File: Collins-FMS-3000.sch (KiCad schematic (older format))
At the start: 25 parts, among them U2 MCP23017_SO, U3 MCP23017_SO, U4 IS31FL3733B

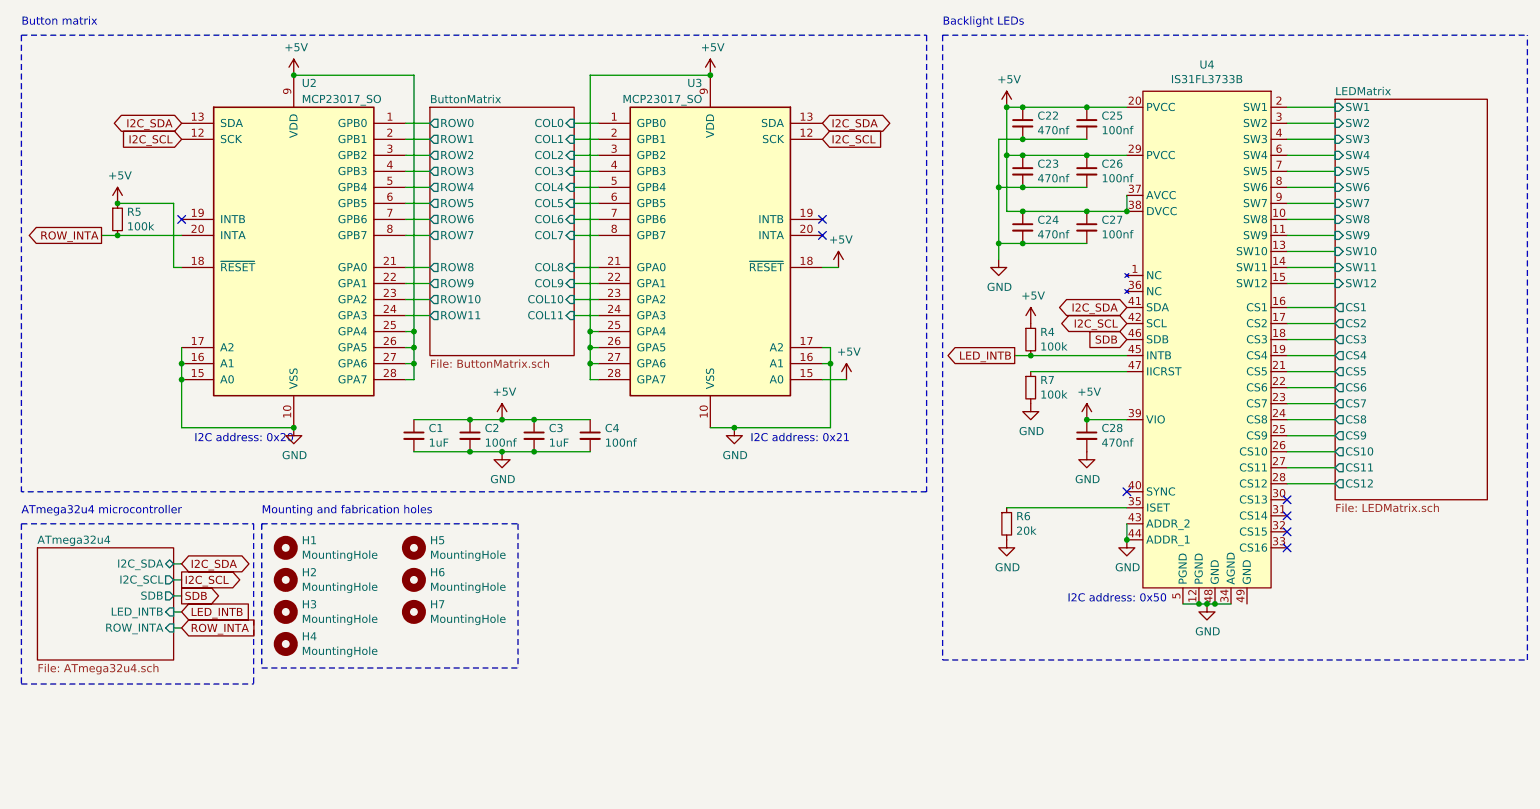
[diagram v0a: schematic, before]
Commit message: Get rid of interrupt pullups, add row pullups
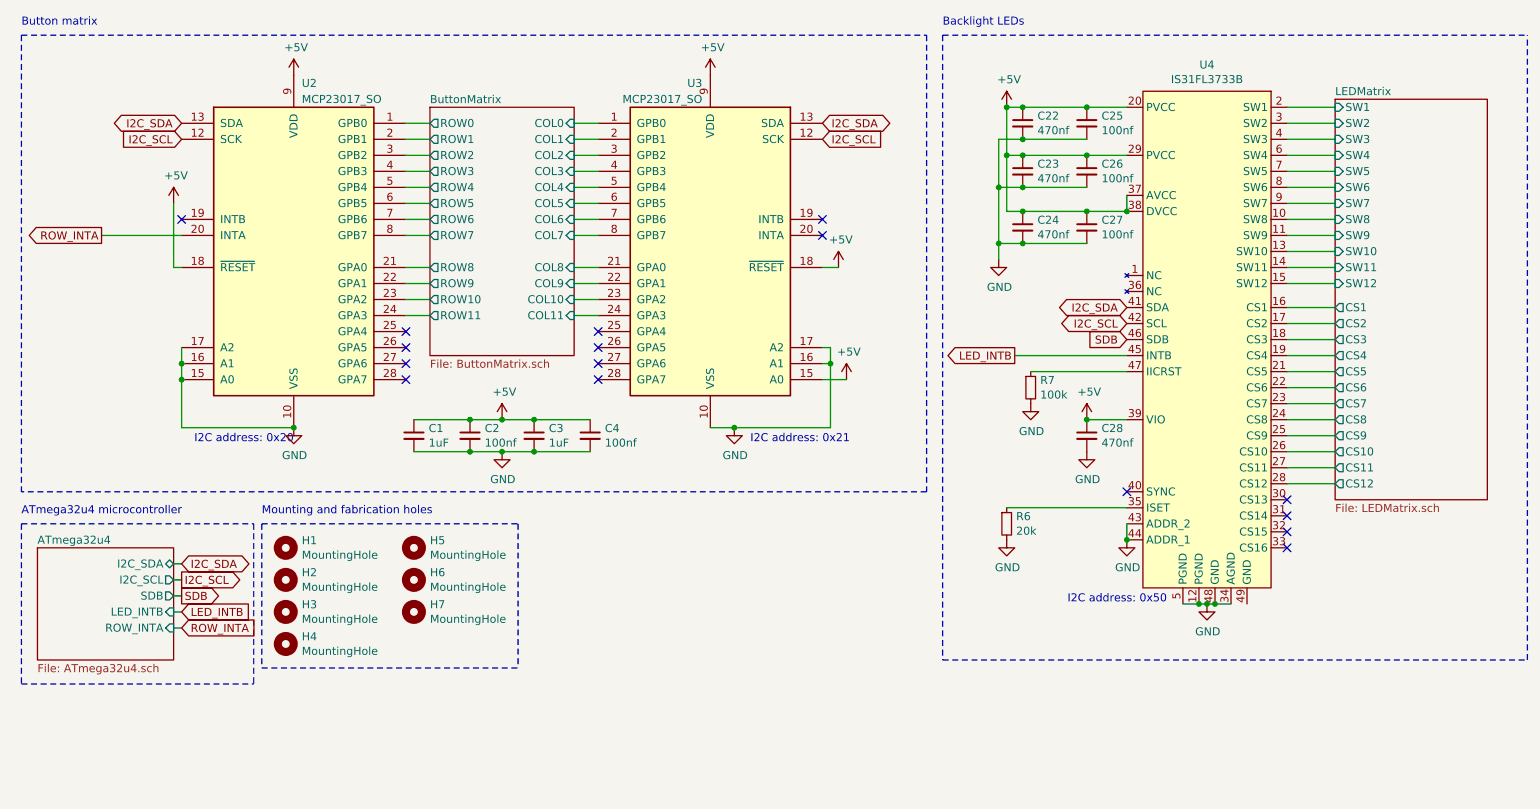
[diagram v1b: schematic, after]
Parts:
- removed R4, R5: 100k, Resistor_SMD:R_0402_1005Metric, symbol Device:R_Small
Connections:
- net +5V: no longer U2.25 (GPA4), U2.26 (GPA5), U2.27 (GPA6), U2.28 (GPA7), U3.25 (GPA4), U3.26 (GPA5), U3.27 (GPA6), U3.28 (GPA7)
- no-connect marks 8 -> 16
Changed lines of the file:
@@
 Text GLabel 6750 2650 0    50   Output ~ 0
 LED_INTB
-Wire Wire Line
-	7450 2650 6850 2650
-$Comp
-L Device:R_Small R4
-U 1 1 61926829
-P 6850 2550
-F 0 "R4" H 6909 2596 50  0000 L CNN
-F 1 "100k" H 6909 2505 50  0000 L CNN
-F 2 "Resistor_SMD:R_0402_1005Metric" H 6850 2550 50  0001 C CNN
-F 3 "~" H 6850 2550 50  0001 C CNN
-	1    6850 2550
-	1    0    0    -1
-$EndComp
-$Comp
-L power:+5V #PWR017
-U 1 1 61927283
-P 6850 2450
-F 0 "#PWR017" H 6850 2300 50  0001 C CNN
-F 1 "+5V" H 6865 2623 50  0000 C CNN
-F 2 "" H 6850 2450 50  0001 C CNN
-F 3 "" H 6850 2450 50  0001 C CNN
-	1    6850 2450
-	1    0    0    -1
-$EndComp
 Text GLabel 1550 4250 2    50   Input ~ 0
 LED_INTB
@@
 ROW_INTA
 $Comp
-L Device:R_Small R5
-U 1 1 619594D7
-P 1150 1800
-F 0 "R5" H 1209 1846 50  0000 L CNN
-F 1 "100k" H 1209 1755 50  0000 L CNN
-F 2 "Resistor_SMD:R_0402_1005Metric" H 1150 1800 50  0001 C CNN
-F 3 "~" H 1150 1800 50  0001 C CNN
-	1    1150 1800
-	1    0    0    -1
-$EndComp
-Wire Wire Line
-	6750 2650 6850 2650
-Connection ~ 6850 2650
-$Comp
 L power:+5V #PWR011
 U 1 1 619844EF
-P 1150 1700
-F 0 "#PWR011" H 1150 1550 50  0001 C CNN
-F 1 "+5V" H 1165 1873 50  0000 C CNN
-F 2 "" H 1150 1700 50  0001 C CNN
-F 3 "" H 1150 1700 50  0001 C CNN
-	1    1150 1700
+P 1500 1700
+F 0 "#PWR011" H 1500 1550 50  0001 C CNN
+F 1 "+5V" H 1515 1873 50  0000 C CNN
+F 2 "" H 1500 1700 50  0001 C CNN
+F 3 "" H 1500 1700 50  0001 C CNN
+	1    1500 1700
 	1    0    0    -1
 $EndComp
@@
 	1550 4350 1500 4350
 Wire Wire Line
-	1050 1900 1150 1900
-Connection ~ 1150 1700
-Connection ~ 1150 1900
-Wire Wire Line
-	1150 1900 1550 1900
-Wire Wire Line
 	1500 1700 1500 2100
 Wire Wire Line
 	1500 2100 1550 2100
-Wire Wire Line
-	1150 1700 1500 1700
-Wire Wire Line
-	2950 2800 3000 2800
-Wire Wire Line
-	3000 2800 3000 2700
-Wire Wire Line
-	3000 2500 2950 2500
-Wire Wire Line
-	2950 2600 3000 2600
-Connection ~ 3000 2600
-Wire Wire Line
-	3000 2600 3000 2500
-Wire Wire Line
-	2950 2700 3000 2700
-Connection ~ 3000 2700
-Wire Wire Line
-	3000 2700 3000 2600
-Wire Wire Line
-	3000 2500 3000 900
-Wire Wire Line
-	3000 900  2250 900
-Connection ~ 3000 2500
-Connection ~ 2250 900
-Wire Wire Line
-	4150 2800 4100 2800
-Wire Wire Line
-	4100 2800 4100 2700
-Wire Wire Line
-	4100 2500 4150 2500
-Wire Wire Line
-	4150 2600 4100 2600
-Connection ~ 4100 2600
-Wire Wire Line
-	4100 2600 4100 2500
-Wire Wire Line
-	4150 2700 4100 2700
-Connection ~ 4100 2700
-Wire Wire Line
-	4100 2700 4100 2600
-Wire Wire Line
-	4100 2500 4100 900
-Wire Wire Line
-	4100 900  4850 900
-Connection ~ 4100 2500
-Connection ~ 4850 900
 Wire Wire Line
 	2950 2400 3100 2400
@@
 Wire Wire Line
 	4000 2400 4150 2400
+NoConn ~ 2950 2500
+NoConn ~ 2950 2600
+NoConn ~ 2950 2700
+NoConn ~ 2950 2800
+NoConn ~ 4150 2500
+NoConn ~ 4150 2600
+NoConn ~ 4150 2700
+NoConn ~ 4150 2800
+Wire Wire Line
+	1050 1900 1550 1900
+Wire Wire Line
+	6750 2650 7450 2650
 $EndSCHEMATC

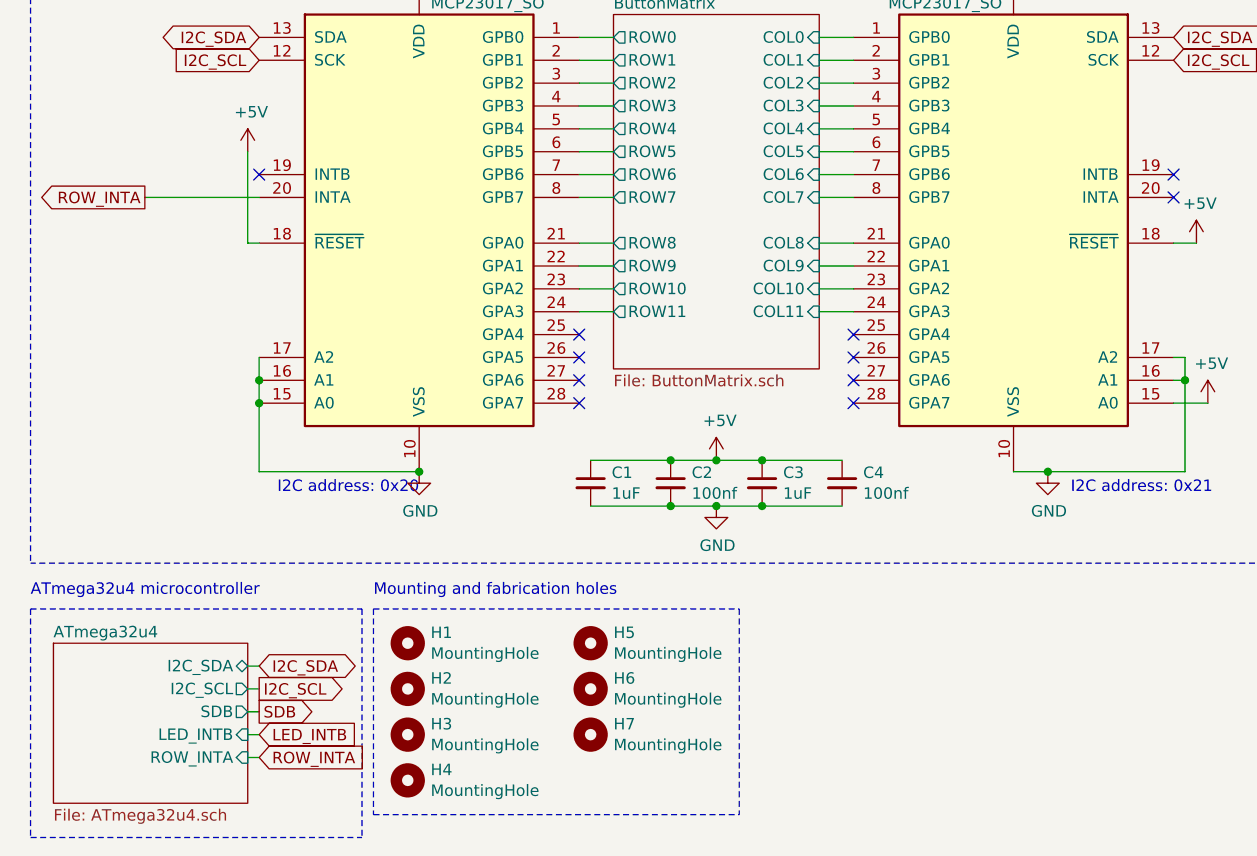
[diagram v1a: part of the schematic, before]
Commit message: Add ROW INTB, new debug header
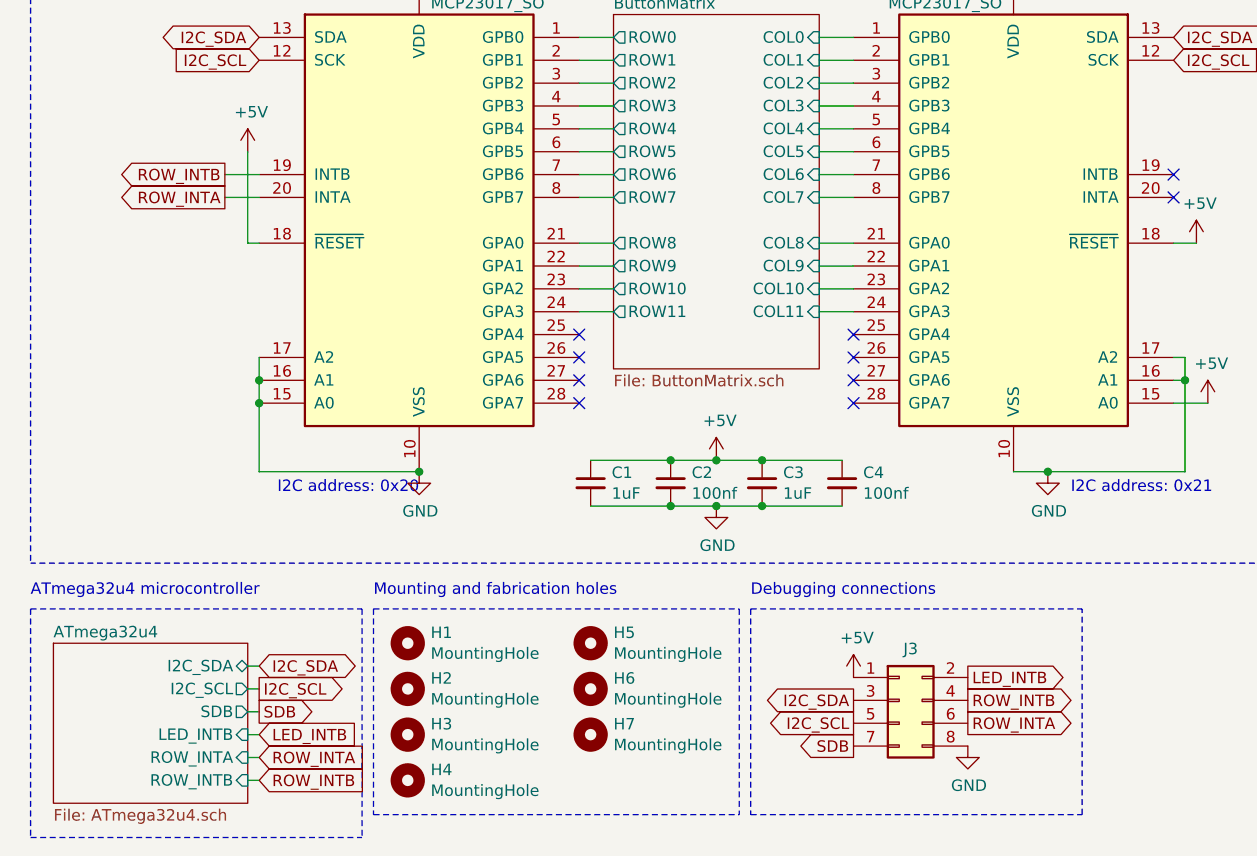
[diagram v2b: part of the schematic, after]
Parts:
- added J3: Conn_02x04_Odd_Even, Connector_PinHeader_2.54mm:PinHeader_2x04_P2.54mm_Vertical, symbol Connector_Generic:Conn_02x04_Odd_Even
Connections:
- net +5V: now also J3.1 (Pin_1)
- net GND: now also J3.8 (Pin_8)
- net I2C_SCL: now also J3.5 (Pin_5)
- net I2C_SDA: now also J3.3 (Pin_3)
- net LED_INTB: now also J3.2 (Pin_2)
- net ROW_INTA: now also J3.6 (Pin_6)
- net SDB: now also J3.7 (Pin_7)
- net ROW_INTB: now reaches U2.19 (INTB)
- net ROW_INTB: now also J3.4 (Pin_4)
- no-connect marks 16 -> 15
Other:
- note added: "Debugging connections"
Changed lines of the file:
@@
 Text GLabel 1550 1300 0    50   Input ~ 0
 I2C_SCL
-NoConn ~ 1550 1800
 $Comp
 L power:GND #PWR02
@@
 F5 "LED_INTB" I R 1500 4250 50
 F6 "ROW_INTA" I R 1500 4350 50
+F7 "ROW_INTB" I R 1500 4450 50
 $EndSheet
 Text GLabel 1550 3950 2    50   BiDi ~ 0
@@
 Wire Wire Line
 	1550 4250 1500 4250
-Text GLabel 1050 1900 0    50   Output ~ 0
+Text GLabel 1400 1900 0    50   Output ~ 0
 ROW_INTA
 $Comp
@@
 NoConn ~ 4150 2800
 Wire Wire Line
-	1050 1900 1550 1900
-Wire Wire Line
 	6750 2650 7450 2650
+Wire Wire Line
+	1400 1900 1550 1900
+Wire Wire Line
+	1550 1800 1400 1800
+Text GLabel 1400 1800 0    50   Output ~ 0
+ROW_INTB
+$Comp
+L power:+5V #PWR017
+U 1 1 61A03F2C
+P 4150 4000
+F 0 "#PWR017" H 4150 3850 50  0001 C CNN
+F 1 "+5V" H 4165 4173 50  0000 C CNN
+F 2 "" H 4150 4000 50  0001 C CNN
+F 3 "" H 4150 4000 50  0001 C CNN
+	1    4150 4000
+	1    0    0    -1
+$EndComp
+Text GLabel 4150 4100 0    50   Output ~ 0
+I2C_SDA
+Text GLabel 4150 4200 0    50   Output ~ 0
+I2C_SCL
+Text GLabel 4150 4300 0    50   Output ~ 0
+SDB
+Text GLabel 4650 4000 2    50   Output ~ 0
+LED_INTB
+Text GLabel 4650 4200 2    50   Output ~ 0
+ROW_INTA
+Text GLabel 4650 4100 2    50   Output ~ 0
+ROW_INTB
+$Comp
+L power:GND #PWR019
+U 1 1 61A0D193
+P 4650 4300
+F 0 "#PWR019" H 4650 4050 50  0001 C CNN
+F 1 "GND" H 4655 4127 50  0000 C CNN
+F 2 "" H 4650 4300 50  0001 C CNN
+F 3 "" H 4650 4300 50  0001 C CNN
+	1    4650 4300
+	1    0    0    -1
+$EndComp
+Text Notes 3700 3650 0    50   ~ 0
+Debugging connections
+Wire Wire Line
+	1500 4450 1550 4450
+Text GLabel 1550 4450 2    50   Input ~ 0
+ROW_INTB
+Wire Notes Line
+	3700 3700 3700 4600
+Wire Notes Line
+	3700 4600 5150 4600
+Wire Notes Line
+	5150 4600 5150 3700
+Wire Notes Line
+	3700 3700 5150 3700
+$Comp
+L Connector_Generic:Conn_02x04_Odd_Even J3
+U 1 1 61A8D1FB
+P 4350 4100
+F 0 "J3" H 4400 4325 50  0000 C CNN
+F 1 "Conn_02x04_Odd_Even" H 4400 4326 50  0001 C CNN
+F 2 "Connector_PinHeader_2.54mm:PinHeader_2x04_P2.54mm_Vertical" H 4350 4100 50  0001 C CNN
+F 3 "~" H 4350 4100 50  0001 C CNN
+	1    4350 4100
+	1    0    0    -1
+$EndComp
 $EndSCHEMATC

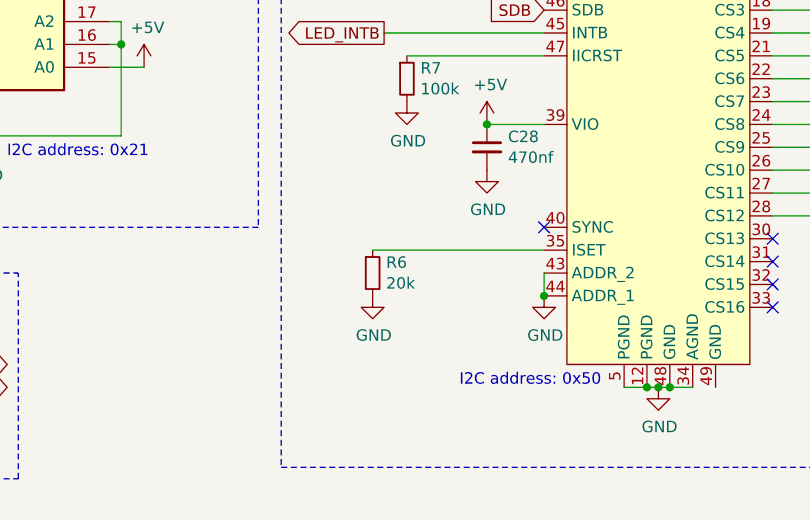
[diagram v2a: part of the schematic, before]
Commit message: Change ISET to 47k Fixes #3
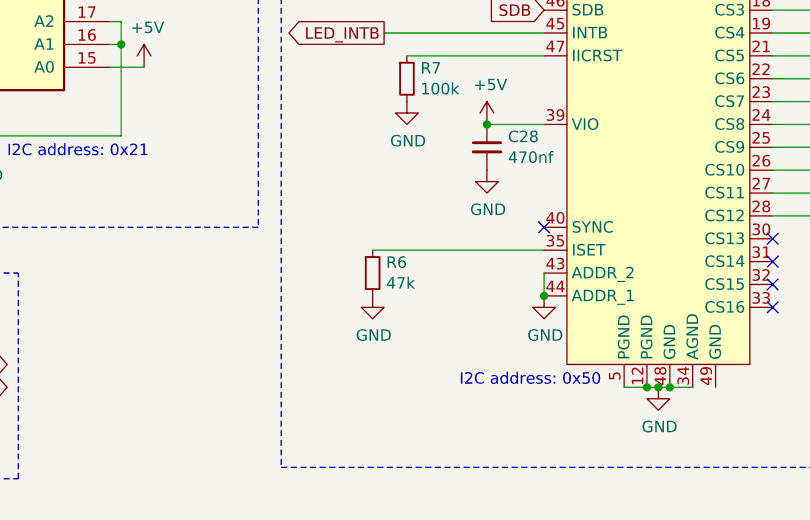
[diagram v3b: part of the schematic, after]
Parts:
- R6: value 20k -> 47k; LCSC C25765 -> C25792
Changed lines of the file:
@@
 P 6700 3700
 F 0 "R6" H 6759 3746 50  0000 L CNN
-F 1 "20k" H 6759 3655 50  0000 L CNN
+F 1 "47k" H 6759 3655 50  0000 L CNN
 F 2 "Resistor_SMD:R_0402_1005Metric" H 6700 3700 50  0001 C CNN
 F 3 "~" H 6700 3700 50  0001 C CNN
 F 4 "0402" H 6700 3700 50  0001 C CNN "JLC"
-F 5 "C25765" H 6700 3700 50  0001 C CNN "LCSC"
+F 5 "C25792" H 6700 3700 50  0001 C CNN "LCSC"
 	1    6700 3700
 	1    0    0    -1

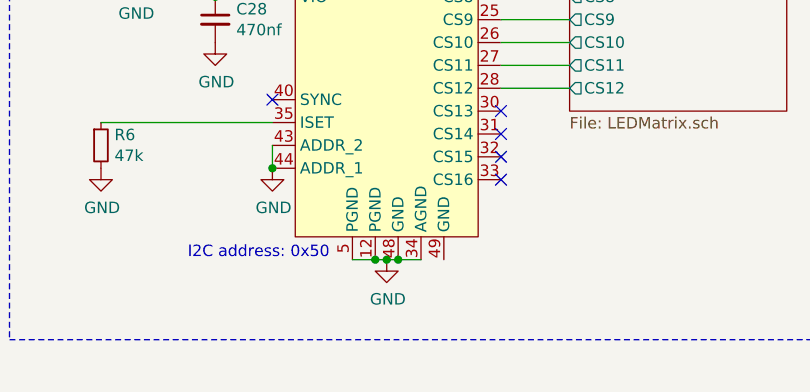
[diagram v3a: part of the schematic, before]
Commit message: Connect thermal pad to ground pins (#5)
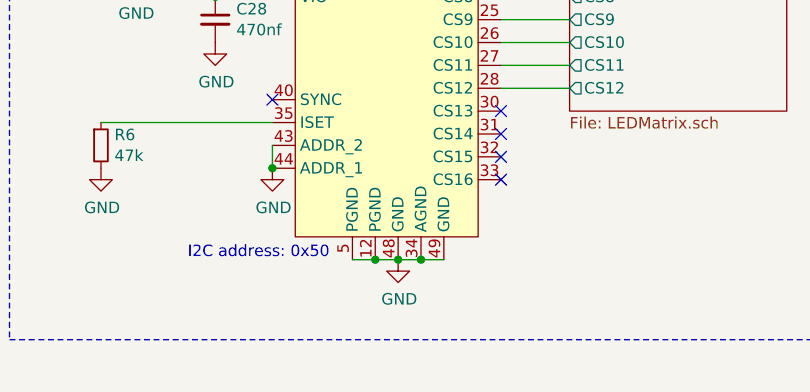
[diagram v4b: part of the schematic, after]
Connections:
- net GND: now also U4.49 (GND)
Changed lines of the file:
@@
 L power:GND #PWR016
 U 1 1 61A720C8
-P 7950 4200
-F 0 "#PWR016" H 7950 3950 50  0001 C CNN
-F 1 "GND" H 7955 4027 50  0000 C CNN
-F 2 "" H 7950 4200 50  0001 C CNN
-F 3 "" H 7950 4200 50  0001 C CNN
-	1    7950 4200
-	1    0    0    -1
-$EndComp
-Connection ~ 7950 4200
+P 8000 4200
+F 0 "#PWR016" H 8000 3950 50  0001 C CNN
+F 1 "GND" H 8005 4027 50  0000 C CNN
+F 2 "" H 8000 4200 50  0001 C CNN
+F 3 "" H 8000 4200 50  0001 C CNN
+	1    8000 4200
+	1    0    0    -1
+$EndComp
 Text GLabel 7450 2550 0    50   Input ~ 0
 SDB
@@
 	6700 3600 7450 3600
 $Comp
-L power:GND #PWR015
-U 1 1 61A9E1C7
-P 7450 3800
-F 0 "#PWR015" H 7450 3550 50  0001 C CNN
-F 1 "GND" H 7455 3627 50  0000 C CNN
-F 2 "" H 7450 3800 50  0001 C CNN
-F 3 "" H 7450 3800 50  0001 C CNN
-	1    7450 3800
-	1    0    0    -1
-$EndComp
-$Comp
 L power:GND #PWR09
 U 1 1 61A9E3B6
@@
 Wire Notes Line
 	550  3700 2000 3700
-Wire Wire Line
-	7800 4200 7900 4200
-Wire Wire Line
-	7950 4200 8000 4200
-$Comp
-L Collins-FMS-3000:IS31FL3733B U4
-U 1 1 61B33736
-P 7950 2150
-F 0 "U4" H 7950 3465 50  0000 C CNN
-F 1 "IS31FL3733B" H 7950 3374 50  0000 C CNN
-F 2 "Package_QFP:TQFP-48-1EP_7x7mm_P0.5mm_EP5x5mm_ThermalVias" H 7950 -350 50  0001 C CNN
-F 3 "https://www.lumissil.com/assets/pdf/core/IS31FL3733B_DS.pdf" H 7950 2150 50  0001 C CNN
-	1    7950 2150
-	1    0    0    -1
-$EndComp
 Connection ~ 7450 1750
-Wire Wire Line
-	7900 4200 7950 4200
-Connection ~ 7900 4200
-Wire Wire Line
-	8000 4200 8100 4200
-Connection ~ 8000 4200
 Wire Notes Line
 	550  650  6200 650
@@
 	1    0    0    -1
 $EndComp
-Wire Wire Line
-	7450 3700 7450 3800
-Connection ~ 7450 3800
 Text Notes 7700 4200 2    50   ~ 0
 I2C address: 0x50
@@
 	1    0    0    -1
 $EndComp
+Connection ~ 8000 4200
+Connection ~ 7900 4200
+Wire Wire Line
+	8000 4200 8100 4200
+Wire Wire Line
+	7800 4200 7900 4200
+$Comp
+L Collins-FMS-3000:IS31FL3733B U4
+U 1 1 61B33736
+P 7950 2150
+F 0 "U4" H 7950 3465 50  0000 C CNN
+F 1 "IS31FL3733B" H 7950 3374 50  0000 C CNN
+F 2 "Package_QFP:TQFP-48-1EP_7x7mm_P0.5mm_EP5x5mm_ThermalVias" H 7950 -350 50  0001 C CNN
+F 3 "https://www.lumissil.com/assets/pdf/core/IS31FL3733B_DS.pdf" H 7950 2150 50  0001 C CNN
+	1    7950 2150
+	1    0    0    -1
+$EndComp
+Wire Wire Line
+	8200 4200 8100 4200
+Connection ~ 8100 4200
+Wire Wire Line
+	7900 4200 8000 4200
+Connection ~ 7450 3800
+Wire Wire Line
+	7450 3700 7450 3800
+$Comp
+L power:GND #PWR015
+U 1 1 61A9E1C7
+P 7450 3800
+F 0 "#PWR015" H 7450 3550 50  0001 C CNN
+F 1 "GND" H 7455 3627 50  0000 C CNN
+F 2 "" H 7450 3800 50  0001 C CNN
+F 3 "" H 7450 3800 50  0001 C CNN
+	1    7450 3800
+	1    0    0    -1
+$EndComp
